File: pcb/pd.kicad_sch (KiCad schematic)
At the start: 7 parts, among them U8 TPS63051RMWR

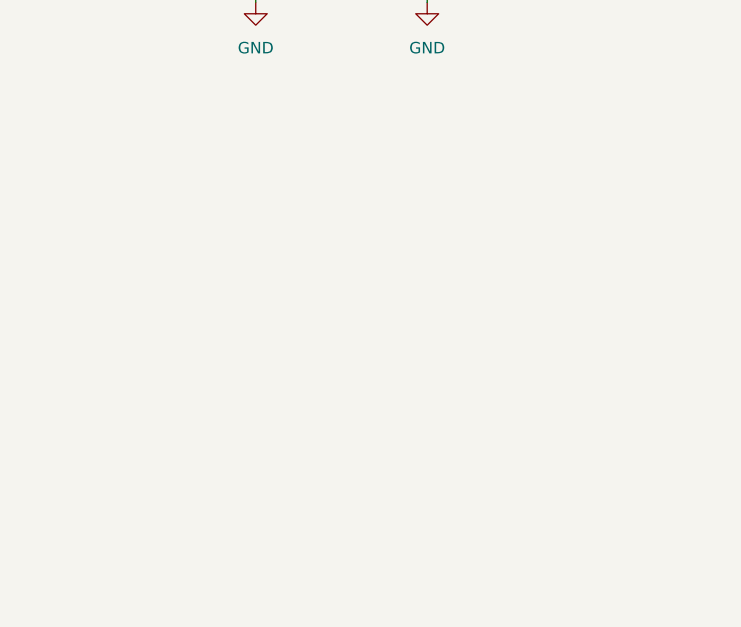
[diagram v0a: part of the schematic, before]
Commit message: feat: 5V power supply
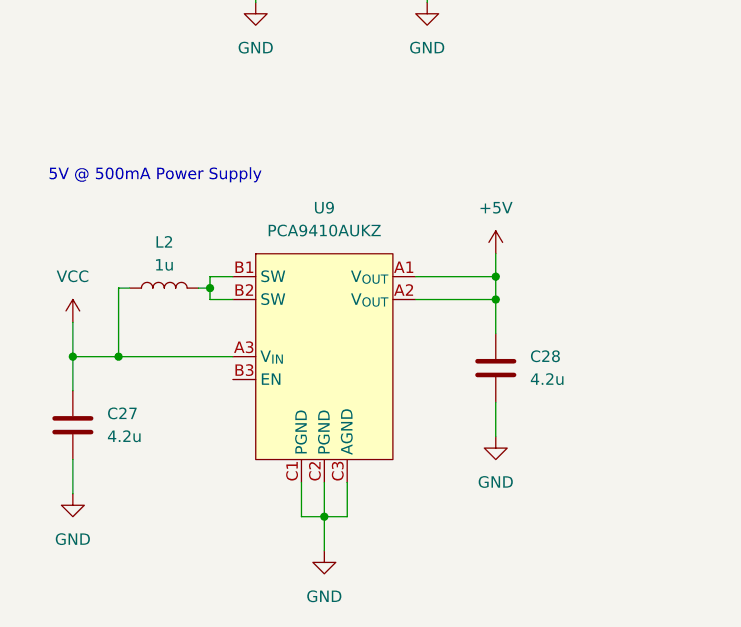
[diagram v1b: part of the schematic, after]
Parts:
- added C27, C28: 4.2u, symbol Device:C
- added L2: 1u, symbol Device:L
- added U9: PCA9410AUKZ, Banshee:WLCSP9_1P24X1P24_NXP, symbol Banshee:PCA9410AUKZ
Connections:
- net GND: now also C27.2, C28.1, U9.C1 (PGND), U9.C2 (PGND), U9.C3 (AGND)
- net VCC: now also C27.1, L2.1, U9.A3 (V_{IN})
- new net: L2.2, U9.B1 (SW), U9.B2 (SW)
- new net +5V: C28.2, U9.A1 (V_{OUT}), U9.A2 (V_{OUT})
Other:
- note added: "5V @ 500mA Power Supply"

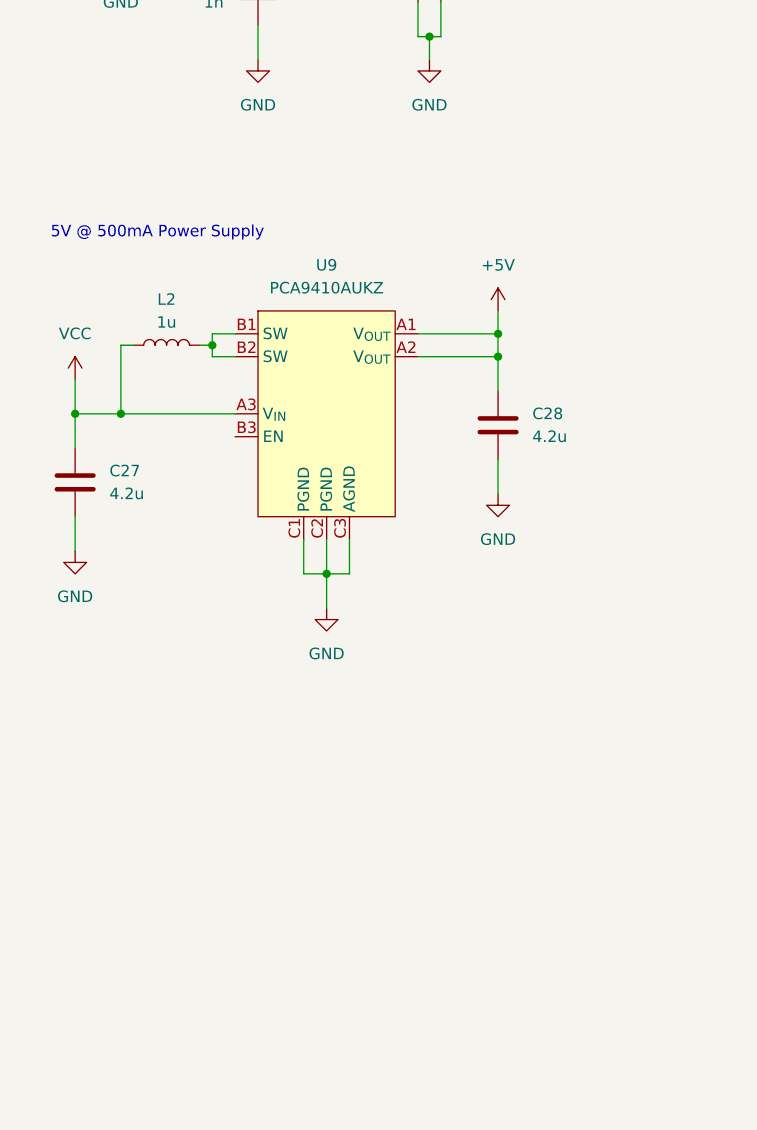
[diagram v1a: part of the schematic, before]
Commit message: feat: 12V 900mA power supply
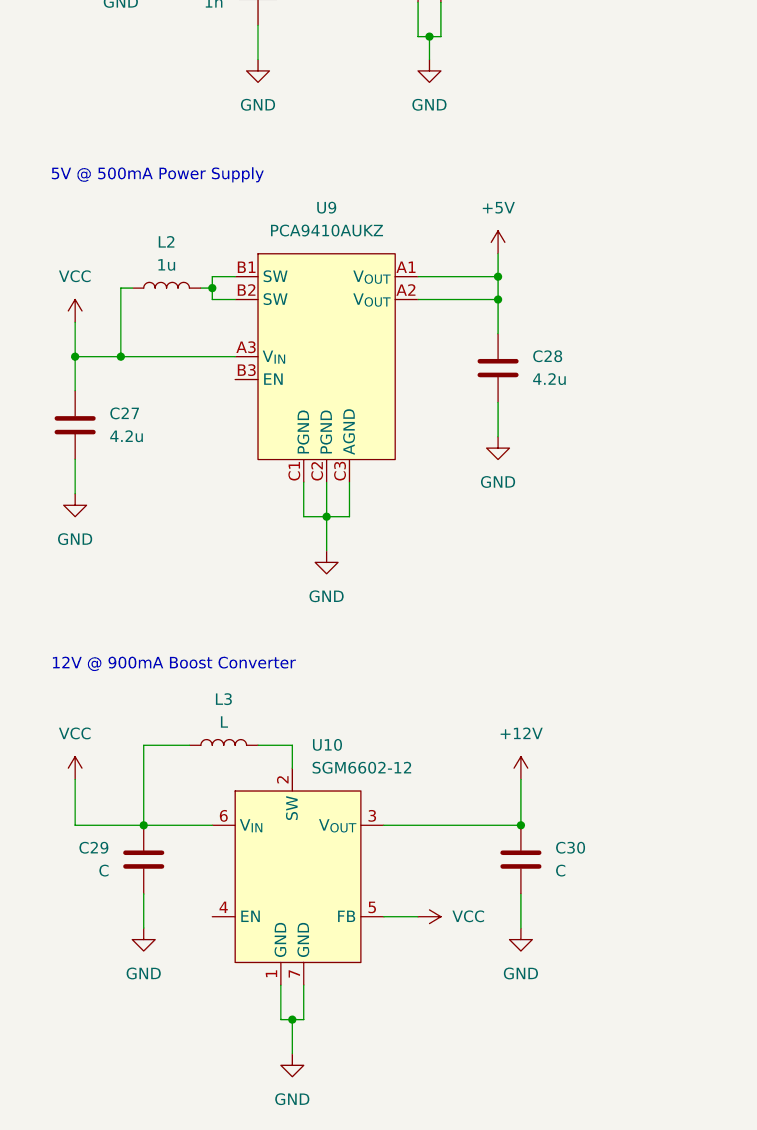
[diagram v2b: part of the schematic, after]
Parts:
- added C29, C30: C, symbol Device:C
- added L3: L, symbol Device:L
- added U10: SGM6602-12, Package_DFN_QFN:DFN-6-1EP_2x2mm_P0.65mm_EP1x1.6mm, symbol Banshee:SGM6602
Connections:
- net GND: now also C29.2, C30.2, U10.1 (GND), U10.7 (GND)
- net VCC: now also C29.1, L3.1, U10.5 (FB), U10.6 (V_{IN})
- new net: L3.2, U10.2 (SW)
- new net +12V: C30.1, U10.3 (V_{OUT})
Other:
- note added: "12V @ 900mA Boost Converter"
- moved on the sheet: C27, C28, L2, U9

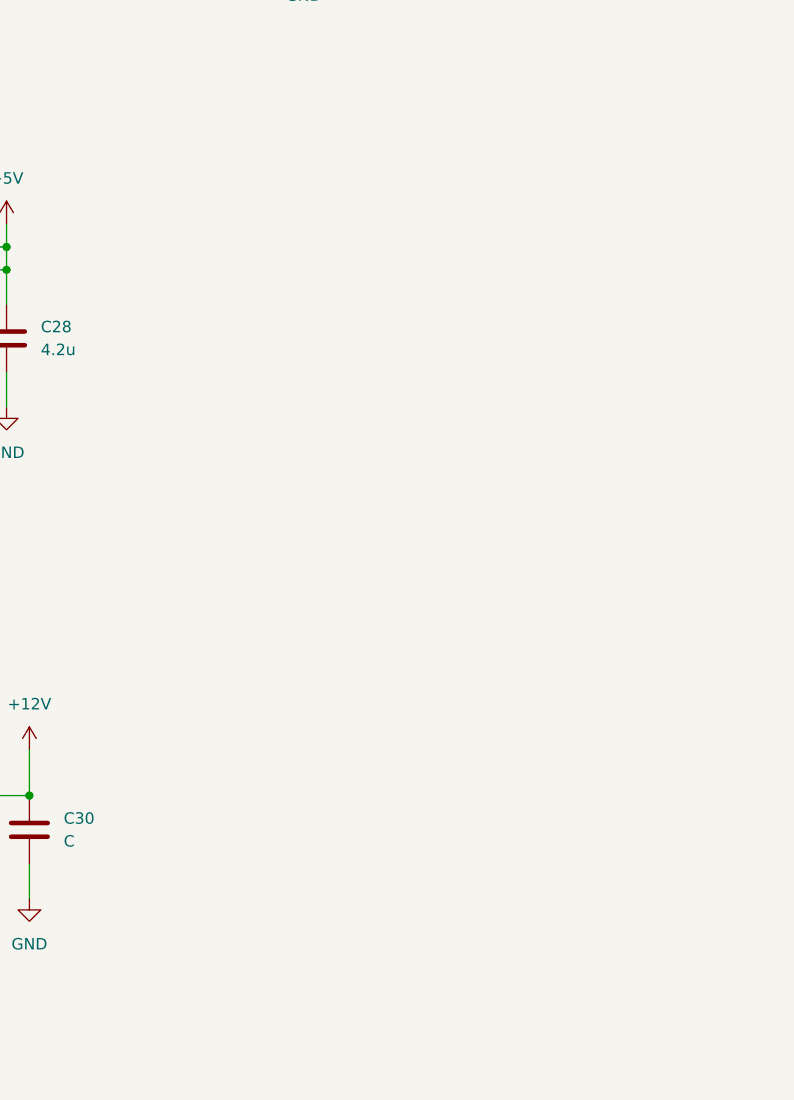
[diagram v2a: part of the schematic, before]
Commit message: feat: battery charging circuit
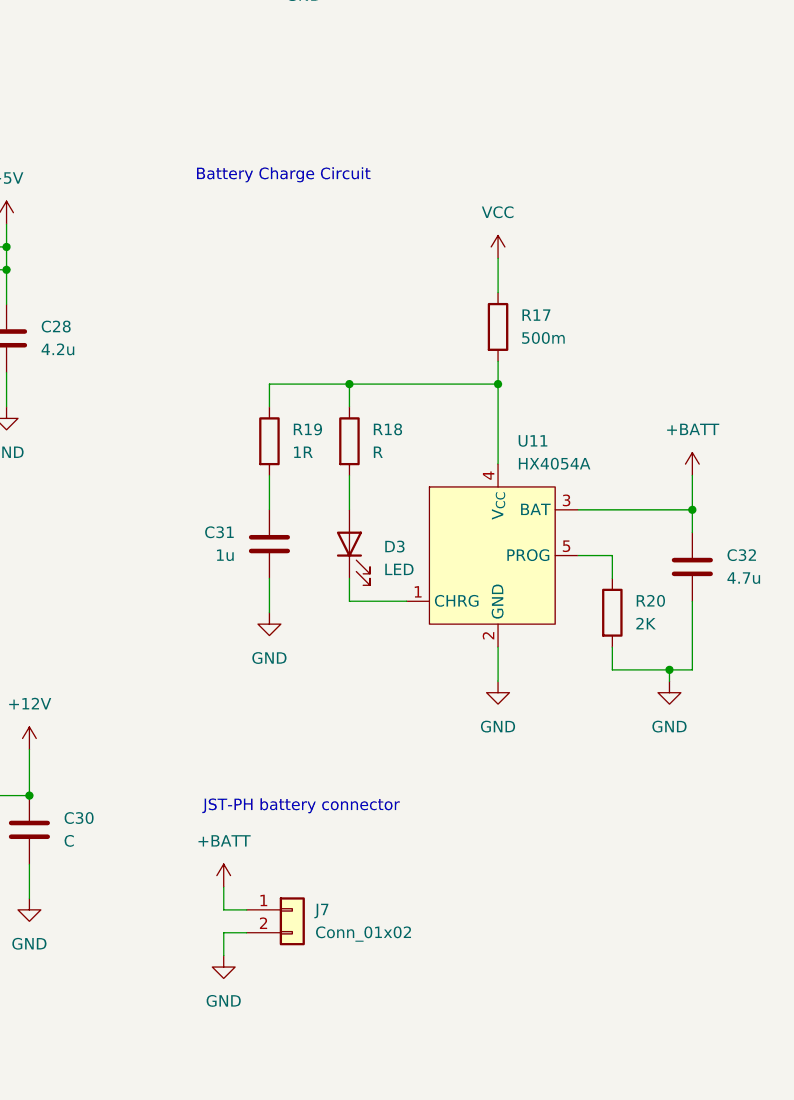
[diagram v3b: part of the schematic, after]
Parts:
- added C31: 1u, symbol Device:C
- added C32: 4.7u, symbol Device:C
- added D3: LED, symbol Device:LED
- added J7: Conn_01x02, Connector_JST:JST_PH_S2B-PH-K_1x02_P2.00mm_Horizontal, symbol Connector_Generic:Conn_01x02
- added R17: 500m, symbol Device:R
- added R18: R, symbol Device:R
- added R19: 1R, symbol Device:R
- added R20: 2K, symbol Device:R
- added U11: HX4054A, Package_TO_SOT_SMD:SOT-23-5_HandSoldering, symbol Banshee:HX4054A
- U10: JLCPCB Part# (none) -> C699551
- U9: JLCPCB Part# (none) -> C2071099
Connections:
- net GND: now also C31.2, C32.2, J7.2 (Pin_2), R20.2, U11.2 (GND)
- net VCC: now also R17.1
- new net: C31.1, R19.2
- new net: D3.1 (K), U11.1 (CHRG)
- new net: R17.2, R18.1, R19.1, U11.4 (V_{CC})
- new net: R20.1, U11.5 (PROG)
- new net: D3.2 (A), R18.2
- new net +BATT: C32.1, J7.1 (Pin_1), U11.3 (BAT)
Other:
- note added: "Battery Charge Circuit"
- note added: "JST-PH battery connector"

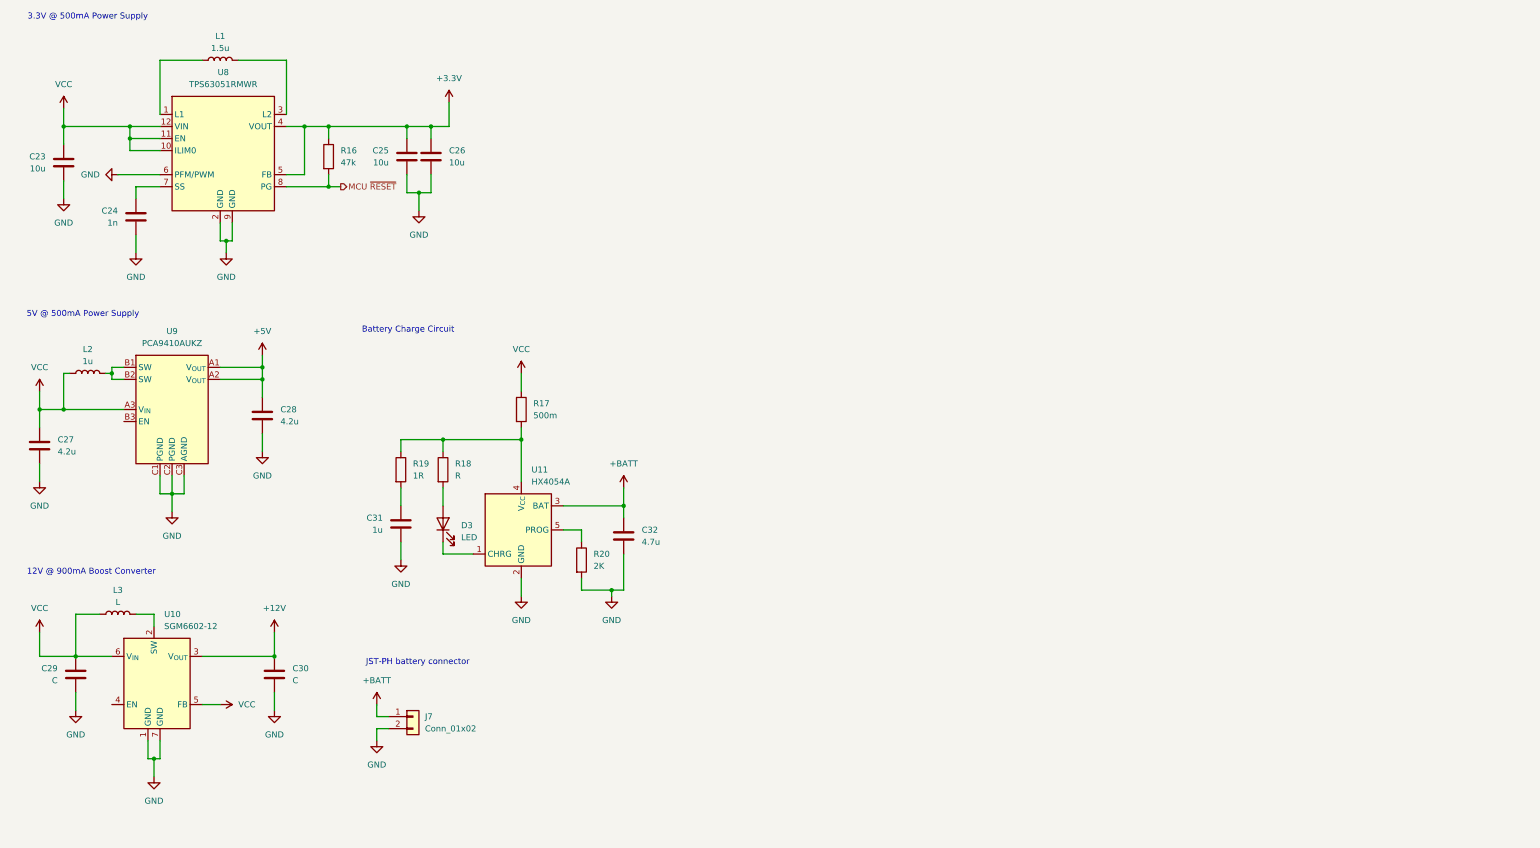
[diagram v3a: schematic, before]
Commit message: feat: fuel gauge circuit
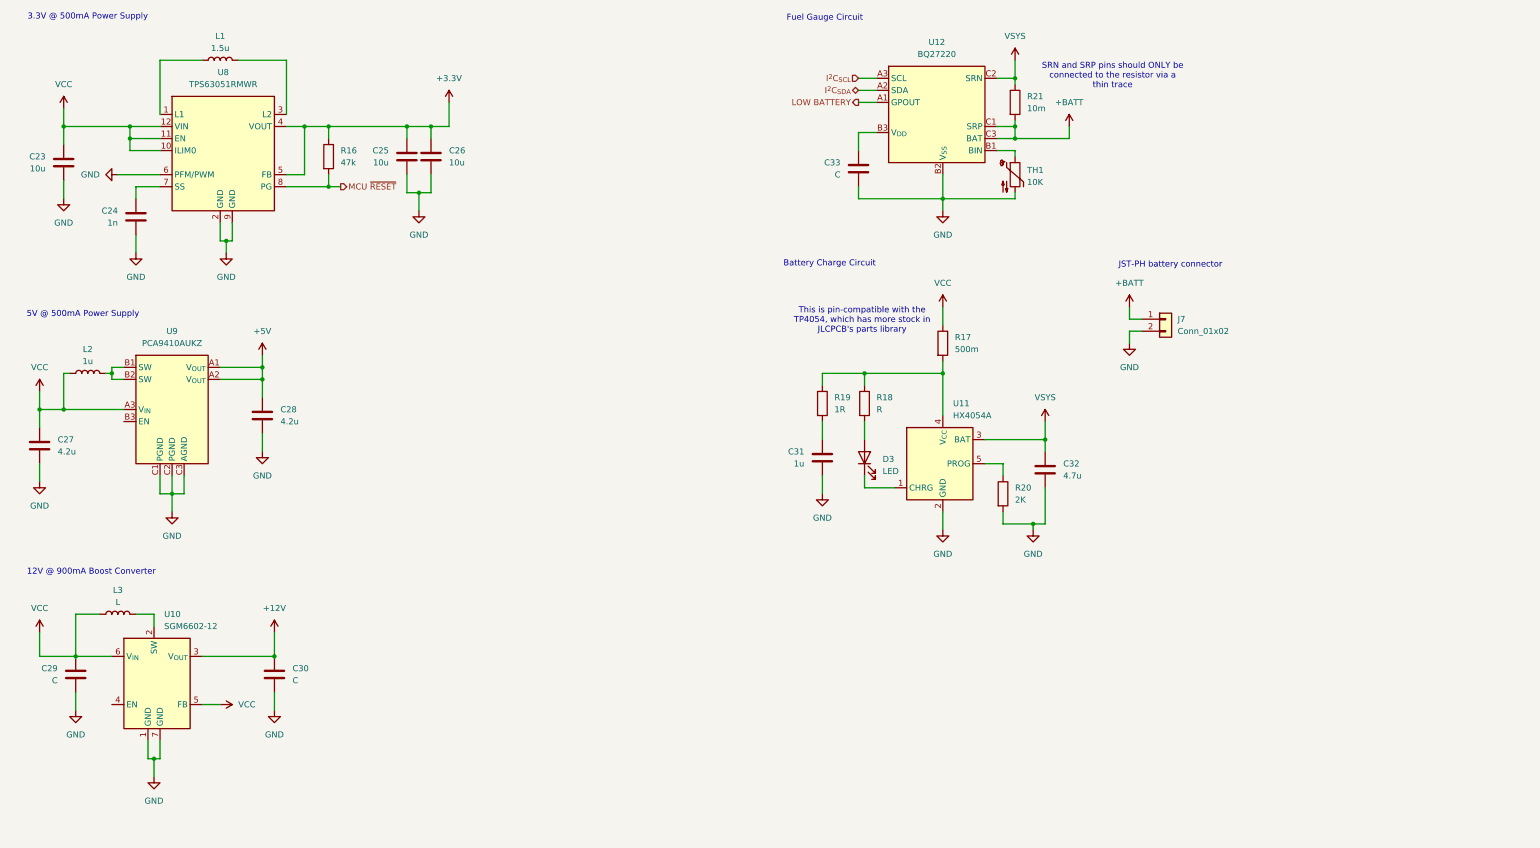
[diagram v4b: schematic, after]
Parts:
- added C33: C, symbol Device:C
- added R21: 10m, symbol Device:R
- added TH1: 10K, symbol Device:Thermistor_NTC
- added U12: BQ27220, Banshee:YZF9_TEX, symbol Banshee:bq27220
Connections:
- net +BATT: now also R21.2, U12.C1 (SRP), U12.C3 (BAT); no longer C32.1, U11.3 (BAT)
- net GND: now also C33.2, TH1.2, U12.B2 (V_{SS})
- new net: TH1.1, U12.B1 (BIN)
- new net: C33.1, U12.B3 (V_{DD})
- new net I^{2}C_{SCL}: U12.A3 (SCL)
- new net I^{2}C_{SDA}: U12.A2 (SDA)
- new net LOW BATTERY: U12.A1 (GPOUT)
- new net VSYS: C32.1, R21.1, U11.3 (BAT), U12.C2 (SRN)
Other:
- note added: "Fuel Gauge Circuit"
- note added: "SRN and SRP pins should ONLY be connected to the resistor via a thin trace"
- note added: "This is pin-compatible with the TP4054, which has more stock in JLCPCB's parts library"
- moved on the sheet: C31, C32, D3, J7, R17, R18, R19, R20, U11
